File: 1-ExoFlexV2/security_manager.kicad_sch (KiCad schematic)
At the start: 13 parts, among them U78 SN74LVC1G32DBVR, U80 SN74LVC1G32DBVR, U81 SN74LVC1G32DBVR, U85 SN74LVC1G32DBVR, U86 SN74LVC1G32DBVR, U87 SN74LVC1G32DBVR, U88 SN74LVC1G32DBVR, U89 SN74LVC1G32DBVR, U90 SN74LVC1G32DBVR, U91 SN74LVC1G32DBVR, U92 SN74LVC1G32DBVR, U93 SN74LVC1G32DBVR

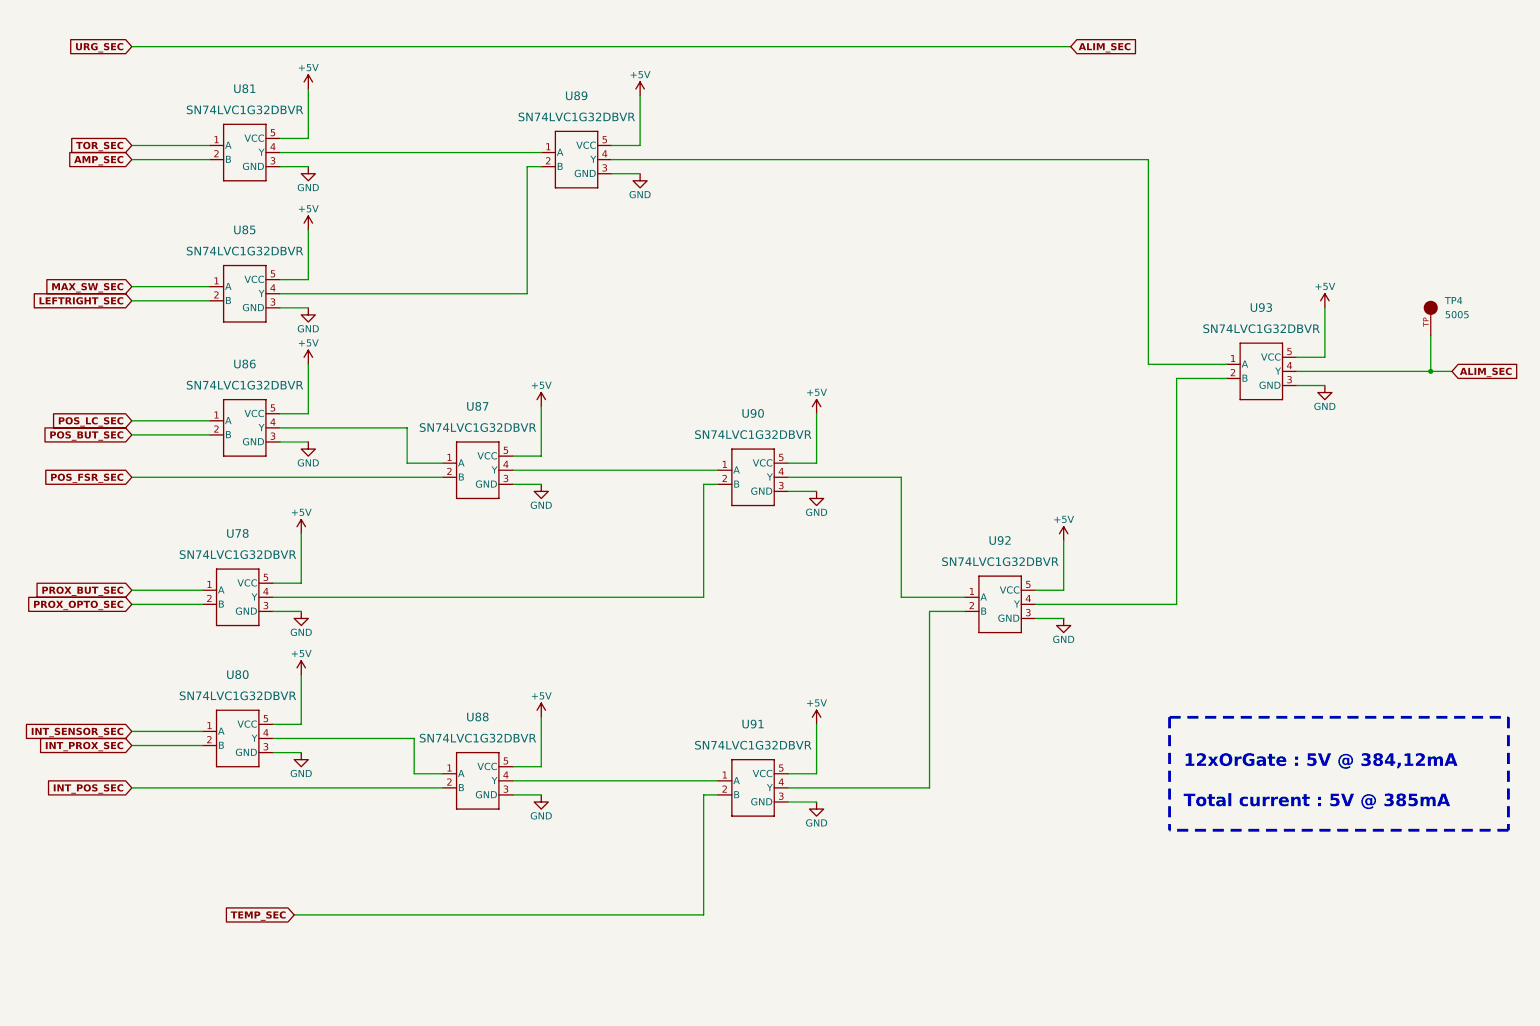
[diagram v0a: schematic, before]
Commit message: Test points et notes
- Ajout de tous les tests point nécessaires
-  Ajoute des sections de notes dans chaque page
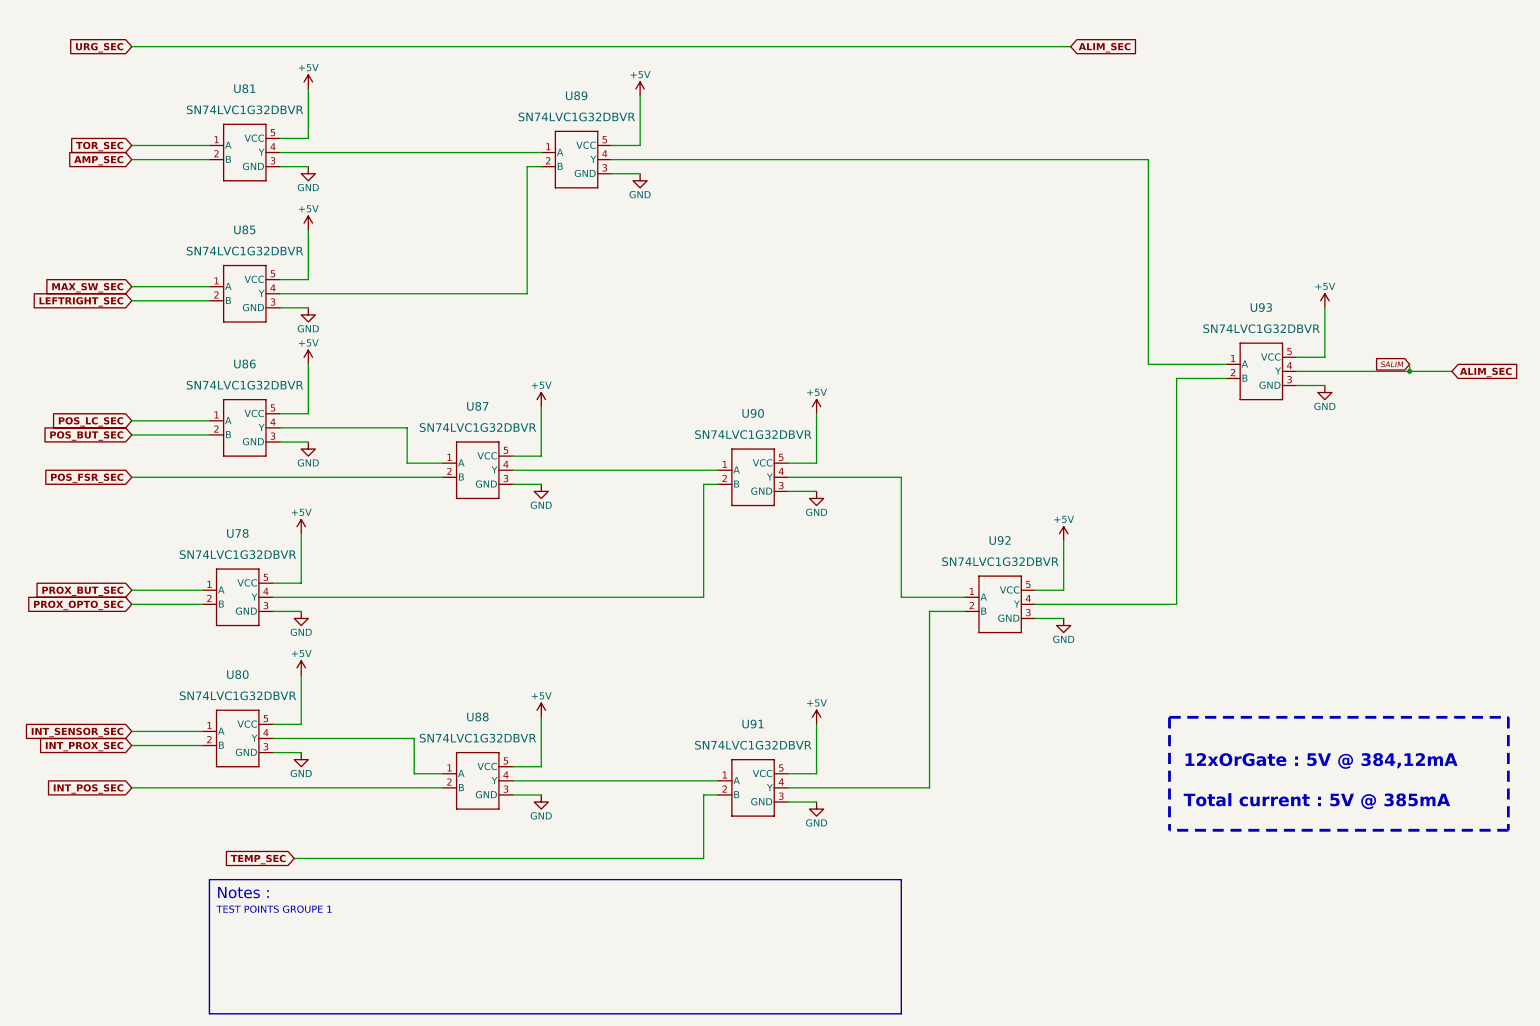
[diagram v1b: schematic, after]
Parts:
- removed TP4: 5005, FootPrint:KEYSTONE_5005, symbol SymLib:5005
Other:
- note added: "Notes :"
- note added: "TEST POINTS GROUPE 1"
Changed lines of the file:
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@@
 (kicad_sch (version 20211123) (generator eeschema)
   (paper "A4")
-  (junction (at 267.97 80.01) (diameter 0) (color 0 0 0 0)
+  (junction (at 264.16 80.01) (diameter 0) (color 0 0 0 0)
   )
   (wire (pts (xy 157.48 143.51) (xy 157.48 152.4))
@@
     (stroke (width 0) (type default) (color 0 0 0 0))
   )
-  (wire (pts (xy 63.5 177.8) (xy 137.16 177.8))
+  (wire (pts (xy 63.5 167.64) (xy 137.16 167.64))
     (stroke (width 0) (type default) (color 0 0 0 0))
   )
@@
   (wire (pts (xy 34.29 154.94) (xy 90.17 154.94))
     (stroke (width 0) (type default) (color 0 0 0 0))
+  )
+  (polyline (pts (xy 48.26 171.45) (xy 172.72 171.45))
+    (stroke (width 0.25) (type solid) (color 0 0 0 0))
   )
   (wire (pts (xy 217.17 41.91) (xy 217.17 78.74))
@@
     (stroke (width 0) (type default) (color 0 0 0 0))
   )
+  (wire (pts (xy 264.16 78.74) (xy 264.16 80.01))
+    (stroke (width 0) (type default) (color 0 0 0 0))
+  )
   (wire (pts (xy 102.87 153.67) (xy 139.7 153.67))
     (stroke (width 0) (type default) (color 0 0 0 0))
@@
     (stroke (width 0) (type default) (color 0 0 0 0))
   )
-  (wire (pts (xy 267.97 73.66) (xy 267.97 80.01))
-    (stroke (width 0) (type default) (color 0 0 0 0))
-  )
   (wire (pts (xy 157.48 101.6) (xy 152.4 101.6))
     (stroke (width 0) (type default) (color 0 0 0 0))
@@
     (stroke (width 0) (type default) (color 0 0 0 0))
   )
+  (polyline (pts (xy 172.72 171.45) (xy 172.72 195.58))
+    (stroke (width 0.25) (type solid) (color 0 0 0 0))
+  )
   (wire (pts (xy 66.04 38.1) (xy 60.96 38.1))
     (stroke (width 0) (type default) (color 0 0 0 0))
@@
     (stroke (width 0) (type default) (color 0 0 0 0))
   )
-  (wire (pts (xy 137.16 177.8) (xy 137.16 156.21))
+  (wire (pts (xy 137.16 167.64) (xy 137.16 156.21))
+    (stroke (width 0) (type default) (color 0 0 0 0))
+  )
+  (wire (pts (xy 264.16 80.01) (xy 271.78 80.01))
     (stroke (width 0) (type default) (color 0 0 0 0))
   )
   (wire (pts (xy 125.73 30.48) (xy 125.73 39.37))
     (stroke (width 0) (type default) (color 0 0 0 0))
+  )
+  (polyline (pts (xy 172.72 195.58) (xy 48.26 195.58))
+    (stroke (width 0.25) (type solid) (color 0 0 0 0))
   )
   (wire (pts (xy 64.77 109.22) (xy 64.77 118.11))
@@
     (stroke (width 0) (type default) (color 0 0 0 0))
   )
-  (wire (pts (xy 267.97 80.01) (xy 271.78 80.01))
+  (wire (pts (xy 243.84 80.01) (xy 264.16 80.01))
     (stroke (width 0) (type default) (color 0 0 0 0))
   )
@@
     (stroke (width 0) (type default) (color 0 0 0 0))
   )
-  (wire (pts (xy 243.84 80.01) (xy 267.97 80.01))
-    (stroke (width 0) (type default) (color 0 0 0 0))
-  )
   (wire (pts (xy 85.09 152.4) (xy 90.17 152.4))
     (stroke (width 0) (type default) (color 0 0 0 0))
@@
   (wire (pts (xy 34.29 144.78) (xy 46.99 144.78))
     (stroke (width 0) (type default) (color 0 0 0 0))
+  )
+  (polyline (pts (xy 48.26 171.45) (xy 48.26 195.58))
+    (stroke (width 0.25) (type solid) (color 0 0 0 0))
   )
   (wire (pts (xy 125.73 39.37) (xy 120.65 39.37))
@@
     (at 223.52 158.75 0)
     (effects (font (size 2.25 2.25) (thickness 0.5) bold) (justify left bottom))
+  )
+  (text "TEST POINTS GROUPE 1" (at 49.53 177.8 0)
+    (effects (font (size 1.27 1.27)) (justify left bottom))
+  )
+  (text "Notes :" (at 49.53 175.26 0)
+    (effects (font (size 2 2)) (justify left bottom))
   )
   (global_label "PROX_BUT_SEC" (shape input) (at 34.29 119.38 180) (fields_autoplaced)
@@
     )
   )
-  (global_label "TEMP_SEC" (shape input) (at 63.5 177.8 180) (fields_autoplaced)
+  (global_label "TEMP_SEC" (shape input) (at 63.5 167.64 180) (fields_autoplaced)
     (effects (font (size 1.27 1.27) bold) (justify right))
-    (property "Intersheet References" "${INTERSHEET_REFS}" (id 0) (at 51.2717 177.927 0)
+    (property "Intersheet References" "${INTERSHEET_REFS}" (id 0) (at 51.2717 167.767 0)
       (effects (font (size 1.27 1.27) bold) (justify right) hide)
     )
@@
     )
   )
+  (global_label "SALIM" (shape input) (at 264.16 78.74 180) (fields_autoplaced)
+    (effects (font (size 1 1) italic) (justify right))
+    (property "Intersheet References" "${INTERSHEET_REFS}" (id 0) (at 257.6707 78.6775 0)
+      (effects (font (size 1 1) italic) (justify right) hide)
+    )
+  )
   (global_label "AMP_SEC" (shape input) (at 34.29 41.91 180) (fields_autoplaced)
     (effects (font (size 1.27 1.27) bold) (justify right))
@@
     (pin "1")
   )
-  (symbol (lib_id "SymLib:5005") (at 267.97 68.58 90) (unit 1)
-    (in_bom yes) (on_board yes) (fields_autoplaced)
-    (property "Reference" "TP4" (id 0) (at 270.51 67.3099 90)
-      (effects (font (size 1.27 1.27)) (justify right))
-    )
-    (property "Value" "5005" (id 1) (at 270.51 69.8499 90)
-      (effects (font (size 1.27 1.27)) (justify right))
-    )
-    (property "Footprint" "FootPrint:KEYSTONE_5005" (id 2) (at 267.97 68.58 0)
-      (effects (font (size 1.27 1.27)) (justify bottom) hide)
-    )
-    (property "Datasheet" "" (id 3) (at 267.97 68.58 0)
-      (effects (font (size 1.27 1.27)) hide)
-    )
-    (property "MF" "Keystone Electronics" (id 4) (at 267.97 68.58 0)
-      (effects (font (size 1.27 1.27)) (justify bottom) hide)
-    )
-    (property "DESCRIPTION" "Compact THM Test Point -Red" (id 5) (at 267.97 68.58 0)
-      (effects (font (size 1.27 1.27)) (justify bottom) hide)
-    )
-    (property "PACKAGE" "NON STANDARD-1 Keystone" (id 6) (at 267.97 68.58 0)
-      (effects (font (size 1.27 1.27)) (justify bottom) hide)
-    )
-    (property "PRICE" "None" (id 7) (at 267.97 68.58 0)
-      (effects (font (size 1.27 1.27)) (justify bottom) hide)
-    )
-    (property "MP" "5005" (id 8) (at 267.97 68.58 0)
-      (effects (font (size 1.27 1.27)) (justify bottom) hide)
-    )
-    (property "AVAILABILITY" "In Stock" (id 9) (at 267.97 68.58 0)
-      (effects (font (size 1.27 1.27)) (justify bottom) hide)
-    )
-    (property "PURCHASE-URL" "https://pricing.snapeda.com/search/part/5005/?ref=eda" (id 10) (at 267.97 68.58 0)
-      (effects (font (size 1.27 1.27)) (justify bottom) hide)
-    )
-    (pin "TP")
-  )
   (symbol (lib_id "power:+5V") (at 201.93 110.49 0) (unit 1)

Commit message: Schématisation terminée
- Schéma terminé
- Passage vers le PCB
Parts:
- U10: renamed from U81; value SN74LVC1G32DBVR -> OR Gate; DESCRIPTION (none) -> OR Gate IC 1 Channel SOT-23-5; MANUFACTURER (none) -> Texas Instruments; PACKAGE (none) -> SC-74A, SOT-753; PART NUMBER (none) -> SN74LVC1G32DBVR; TYPE (none) -> SMD
- U11: renamed from U85; value SN74LVC1G32DBVR -> OR Gate; DESCRIPTION (none) -> OR Gate IC 1 Channel SOT-23-5; MANUFACTURER (none) -> Texas Instruments; PACKAGE (none) -> SC-74A, SOT-753; PART NUMBER (none) -> SN74LVC1G32DBVR; TYPE (none) -> SMD
- U12: renamed from U86; value SN74LVC1G32DBVR -> OR Gate; DESCRIPTION (none) -> OR Gate IC 1 Channel SOT-23-5; MANUFACTURER (none) -> Texas Instruments; PACKAGE (none) -> SC-74A, SOT-753; PART NUMBER (none) -> SN74LVC1G32DBVR; TYPE (none) -> SMD
- U13: renamed from U87; value SN74LVC1G32DBVR -> OR Gate; DESCRIPTION (none) -> OR Gate IC 1 Channel SOT-23-5; MANUFACTURER (none) -> Texas Instruments; PACKAGE (none) -> SC-74A, SOT-753; PART NUMBER (none) -> SN74LVC1G32DBVR; TYPE (none) -> SMD
- U14: renamed from U88; value SN74LVC1G32DBVR -> OR Gate; DESCRIPTION (none) -> OR Gate IC 1 Channel SOT-23-5; MANUFACTURER (none) -> Texas Instruments; PACKAGE (none) -> SC-74A, SOT-753; PART NUMBER (none) -> SN74LVC1G32DBVR; TYPE (none) -> SMD
- U15: renamed from U89; value SN74LVC1G32DBVR -> OR Gate; DESCRIPTION (none) -> OR Gate IC 1 Channel SOT-23-5; MANUFACTURER (none) -> Texas Instruments; PACKAGE (none) -> SC-74A, SOT-753; PART NUMBER (none) -> SN74LVC1G32DBVR; TYPE (none) -> SMD
- U16: renamed from U90; value SN74LVC1G32DBVR -> OR Gate; DESCRIPTION (none) -> OR Gate IC 1 Channel SOT-23-5; MANUFACTURER (none) -> Texas Instruments; PACKAGE (none) -> SC-74A, SOT-753; PART NUMBER (none) -> SN74LVC1G32DBVR; TYPE (none) -> SMD
- U17: renamed from U91; value SN74LVC1G32DBVR -> OR Gate; DESCRIPTION (none) -> OR Gate IC 1 Channel SOT-23-5; MANUFACTURER (none) -> Texas Instruments; PACKAGE (none) -> SC-74A, SOT-753; PART NUMBER (none) -> SN74LVC1G32DBVR; TYPE (none) -> SMD
- U18: renamed from U92; value SN74LVC1G32DBVR -> OR Gate; DESCRIPTION (none) -> OR Gate IC 1 Channel SOT-23-5; MANUFACTURER (none) -> Texas Instruments; PACKAGE (none) -> SC-74A, SOT-753; PART NUMBER (none) -> SN74LVC1G32DBVR; TYPE (none) -> SMD
- U19: renamed from U93; value SN74LVC1G32DBVR -> OR Gate; DESCRIPTION (none) -> OR Gate IC 1 Channel SOT-23-5; MANUFACTURER (none) -> Texas Instruments; PACKAGE (none) -> SC-74A, SOT-753; PART NUMBER (none) -> SN74LVC1G32DBVR; TYPE (none) -> SMD
- U8: renamed from U78; value SN74LVC1G32DBVR -> OR Gate; DESCRIPTION (none) -> OR Gate IC 1 Channel SOT-23-5; MANUFACTURER (none) -> Texas Instruments; PACKAGE (none) -> SC-74A, SOT-753; PART NUMBER (none) -> SN74LVC1G32DBVR; TYPE (none) -> SMD
- U9: renamed from U80; value SN74LVC1G32DBVR -> OR Gate; DESCRIPTION (none) -> OR Gate IC 1 Channel SOT-23-5; MANUFACTURER (none) -> Texas Instruments; PACKAGE (none) -> SC-74A, SOT-753; PART NUMBER (none) -> SN74LVC1G32DBVR; TYPE (none) -> SMD
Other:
- note added: "12xOrGate : 5V @ 384,12mA Total current : 5V @ 389mA"
- note removed: "12xOrGate : 5V @ 384,12mA Total current : 5V @ 385mA"
